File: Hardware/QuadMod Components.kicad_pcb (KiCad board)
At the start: 2 copper layers, 70.6 x 100 mm, 120 parts, among them J1 Conn_01x08_Pin, J2 Conn_01x08_Pin, J3 Conn_01x08_Pin, J4 Conn_01x08_Pin, J5 Eurorack_10_pin_power, J6 USB_B_Micro, J7 Prog_Header, J8 Extra_Outs, U1 LD1117-3.3-4Tab, U2 STM32H563VIT, U3 TL072, U4 MCP6004, U5 TPS561201, U6 MCP6004, U7 MCP6002-xSN, U8 STF202-22T1G, U9 AK4619VN, Y1 8MHz 20pF

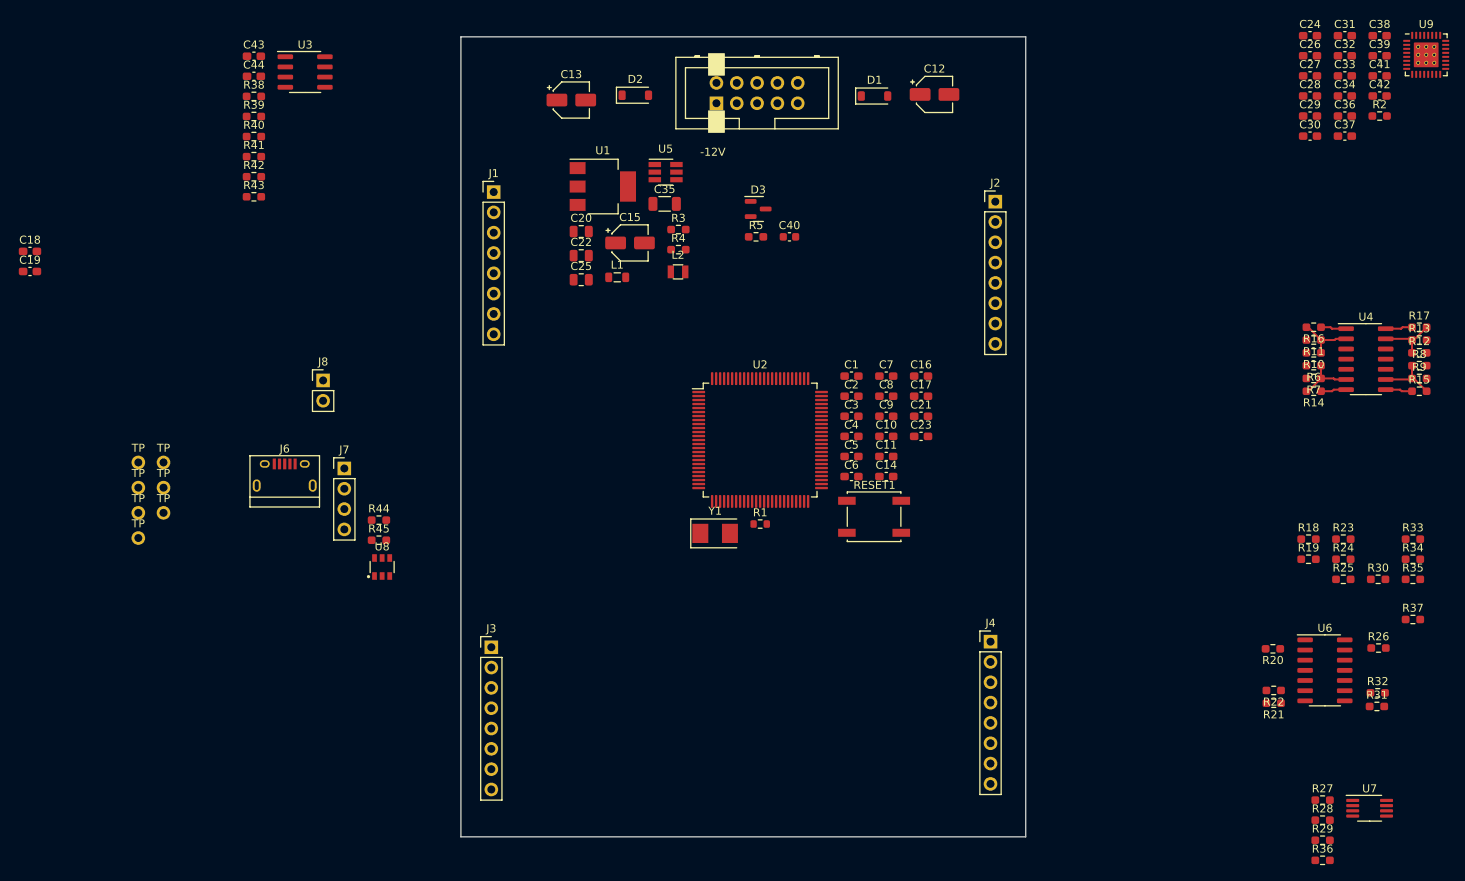
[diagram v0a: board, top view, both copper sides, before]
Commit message: Preliminary component routing
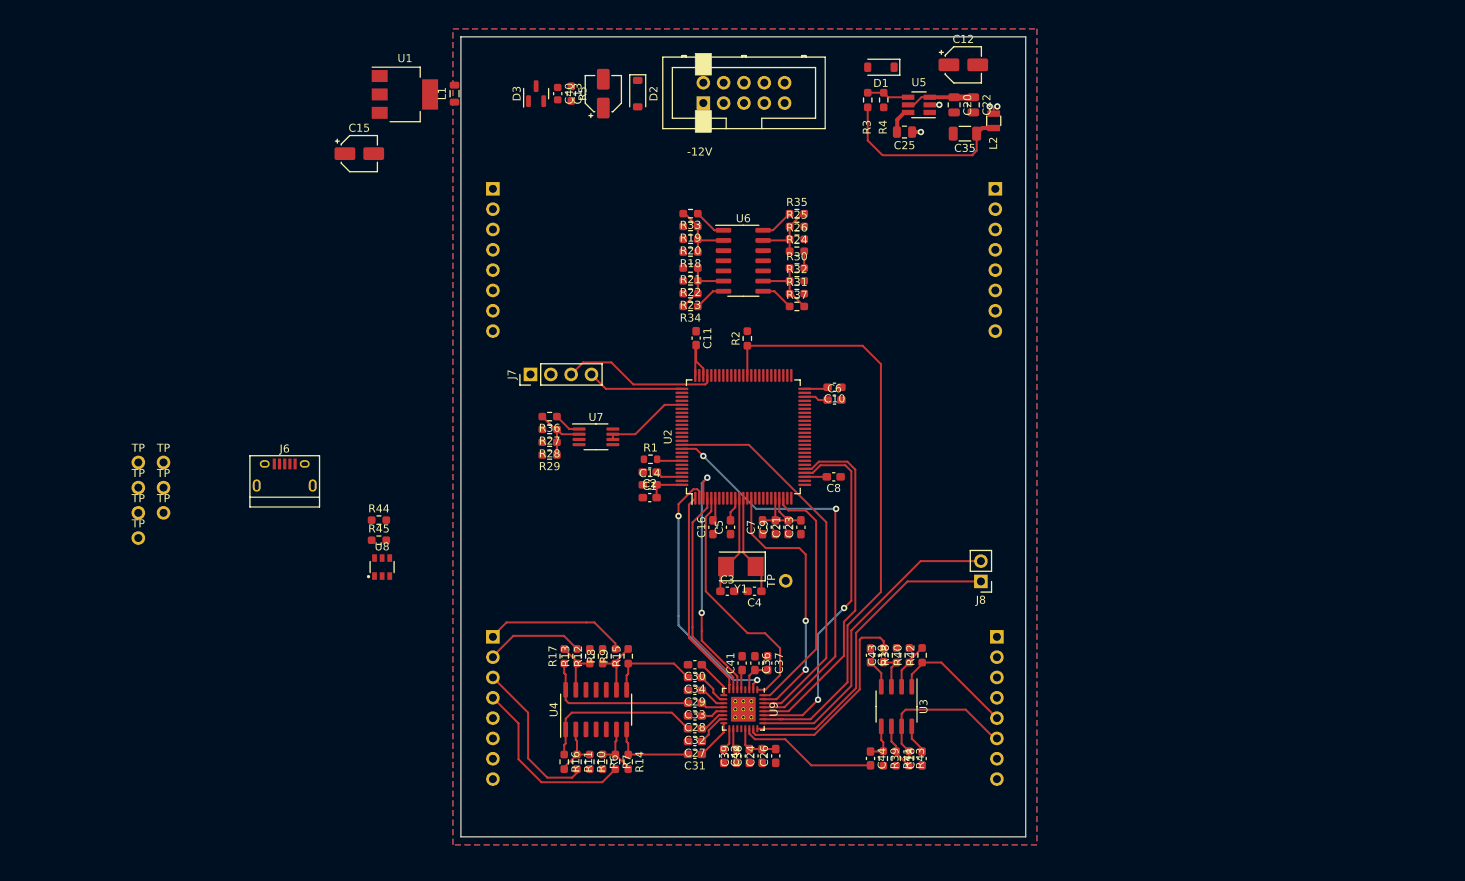
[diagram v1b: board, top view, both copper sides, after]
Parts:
- removed C17: 100nF, Capacitor_SMD:C_0603_1608Metric_Pad1.08x0.95mm_HandSolder
- removed RESET1: SW_Push, Custom_Footprints:SW_SPST_EVQQ2
- added TP8: Reset, Custom_Footprints:1mm_Test_Point, F.Cu at (140.6, 118.0)
- J1, J2, J3, J4: moved to B.Cu
- moved C18 128.3 mm to (157.7, 140.2), turned to 90 degrees
- moved C31 121.1 mm to (129.2, 139.7), turned to 180 degrees
- moved C38 119.6 mm to (136.1, 139.9), turned to 90 degrees
- moved C39 118.8 mm to (134.4, 139.9), turned to 90 degrees
- moved U9 118.2 mm to (135.3, 134.1), turned to -90 degrees
- moved C32 116.9 mm to (129.2, 136.5), turned to 180 degrees
- moved C42 116.3 mm to (132.8, 139.9), turned to -90 degrees
- moved C19 115.5 mm to (151.2, 127.3), turned to -90 degrees
- moved C44 114.9 mm to (151.2, 140.2), turned to -90 degrees
- moved R17 114.5 mm to (112.9, 127.4), turned to 90 degrees
- moved C27 113.3 mm to (129.2, 138.1), turned to 180 degrees
- moved C24 113.1 mm to (137.7, 139.9), turned to 90 degrees
- moved C33 112.9 mm to (129.2, 133.3), turned to 180 degrees
- moved R13 112.5 mm to (114.5, 127.4), turned to 90 degrees
- moved R39 112.4 mm to (152.8, 140.2), turned to -90 degrees
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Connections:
- C43 pad 2: /Audio_Out1 -> /Audio_Out2
- C44 pad 2: /Audio_Out2 -> /Audio_Out1
- J3 pad 1: /FX_TYPE -> /IN4
- J3 pad 2: /CLOCK -> /IN3
- J3 pad 3: /DELAY_LED -> /IN2
- J3 pad 4: /FX_LED -> /IN1
- J4 pad 1: /IN1 -> /FX_TYPE
- J4 pad 2: /IN2 -> /CLOCK
- J4 pad 3: /IN3 -> /DELAY_LED
- J4 pad 4: /IN4 -> /FX_LED
- J4 pad 5: /OUT_AMP1 -> /OUT_AMP2
- J4 pad 6: /OUT_AMP2 -> /OUT_AMP1
- R42 pad 1: /OUT_AMP1 -> /OUT_AMP2
- R43 pad 1: /OUT_AMP2 -> /OUT_AMP1
- U2 pad 15: /LFO_RANGE -> /SAI2_SD_A
- U2 pad 16: /Delay_Time -> unconnected-(U2-PC1-Pad16)
- U2 pad 17: /FX_MIX -> unconnected-(U2-PC2_C-Pad17)
- U2 pad 18: /FX_Feedback -> unconnected-(U2-PC3_C-Pad18)
- U2 pad 23: unconnected-(U2-PA0-Pad23) -> /SAI2_SD_B
- U2 pad 24: unconnected-(U2-PA1-Pad24) -> /FX_Feedback
- U2 pad 25: unconnected-(U2-PA2-Pad25) -> /LFO_RANGE
- U2 pad 26: unconnected-(U2-PA3-Pad26) -> /FX_MIX
- U2 pad 29: unconnected-(U2-PA4-Pad29) -> /SPI1_NSS
- U2 pad 31: unconnected-(U2-PA6-Pad31) -> /Delay_Time
- U2 pad 42: /SAI2_SD_B -> unconnected-(U2-PE11-Pad42)
- U2 pad 58: /SAI2_SD_A -> unconnected-(U2-PD11-Pad58)
- U2 pad 77: /SPI1_NSS -> unconnected-(U2-PA15-Pad77)
- U3 pad 1: /OUT_AMP1 -> /OUT_AMP2
- U3 pad 7: /OUT_AMP2 -> /OUT_AMP1
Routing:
- net /PDN: track 0.00 -> 75.8 mm
- net /SPI1_MOSI: track 0.00 -> 52.6 mm, vias 0 -> 2
- net +3.3V: track 0.00 -> 52.0 mm
- net /SPI1_MISO: track 0.00 -> 49.3 mm
- net /SPI1_NSS: track 0.00 -> 44.5 mm, vias 0 -> 2
- net /SPI1_SCK: track 0.00 -> 44.0 mm
- net /Audio_Out4: track 0.00 -> 39.7 mm
- net /Audio_Out3: track 0.00 -> 39.6 mm
- net /SAI2_SD_A: track 0.00 -> 33.6 mm, vias 0 -> 2
- net /SAI1_SD_B: track 0.00 -> 33.6 mm, vias 0 -> 2
- net /SAI1_FS_A: track 0.00 -> 31.4 mm, vias 0 -> 2
- net /SAI1_SD_A: track 0.00 -> 31.1 mm
- net /SAI2_SD_B: track 0.00 -> 30.9 mm
- net /SAI1_SCK_A: track 0.00 -> 26.8 mm
- net /Audio_Out2: track 0.00 -> 26.7 mm
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- added copper zone on In1.Cu, net /VSW
- added copper zone on B.Cu, net GND
- added copper zone on F.Cu, net GND
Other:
- copper layers 2 -> 4

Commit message: First pass signal routing of component board
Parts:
- moved R45 74.6 mm to (159.3, 85.9)
- moved R44 74.3 mm to (159.3, 84.3)
- moved J6 26.7 mm to (104.2, 109.4), turned to -90 degrees
- moved U8 21.5 mm to (110.5, 109.4), turned to 90 degrees
- moved J8 2.00 mm to (167.0, 118.1)
- moved C11 0.55 mm to (129.3, 88.2)
- moved R2 0.50 mm to (135.8, 88.2)
- moved R1 0.10 mm to (123.6, 102.8)
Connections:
- J1 pad 1: /DLY_TIME_POT -> /DLY_TIME_CV
- J1 pad 2: /DLY_FILTER_CV -> /DLY_TIME_POT
- J1 pad 3: /DLY_FILTER_POT -> /DLY_FILTER_CV
- J1 pad 4: /LFO_SPEED_CV -> /DLY_FILTER_POT
- J1 pad 5: /LFO_SPEED_POT -> /LFO_BASEFREQ_CV
- J1 pad 6: /LFO_RANGE -> /LFO_BASEFREQ_POT
- J1 pad 7: +3.3VA -> /CLOCK
- J2 pad 2: /DLY_FEEDBACK -> /FX_FEEDBACK_CV
- J2 pad 3: /DLY_TIME_CV -> /FX_FEEDBACK_POT
- J2 pad 4: /FX_FEEDBACK_CV -> /LFO_SPEED_POT
- J2 pad 5: /FX_FEEDBACK_POT -> /LFO_SPEED_CV
- J2 pad 6: /LFO_BASEFREQ_CV -> /DELAY_LED
- J2 pad 7: /LFO_BASEFREQ_POT -> /FX_LED
- J3 pad 1: /IN4 -> /FX_TYPE
- J3 pad 2: /IN3 -> /LFO_RANGE
- J3 pad 3: /IN2 -> /IN4
- J3 pad 4: /IN1 -> /IN3
- J3 pad 5: /DLY_MIX -> /IN2
- J3 pad 6: /FX_MIX -> /IN1
- J4 pad 1: /FX_TYPE -> /DLY_FEEDBACK
- J4 pad 2: /CLOCK -> /DLY_MIX
- J4 pad 3: /DELAY_LED -> unconnected-(J4-Pin_3-Pad3)
- J4 pad 4: /FX_LED -> /FX_MIX
- U2 pad 24: /FX_Feedback -> /LFO_Base_Freq
- U2 pad 31: /Delay_Time -> /DLY_FEEDBACK
- U2 pad 32: /Delay_Filter -> /DLY_MIX
- U2 pad 34: /DLY_MIX -> /FX_Feedback
- U2 pad 35: /DLY_FEEDBACK -> /Delay_Time
- U2 pad 36: /LFO_Base_Freq -> /Delay_Filter
- U2 pad 78: /FX_TYPE -> unconnected-(U2-PC10-Pad78)
- U2 pad 87: unconnected-(U2-PD6-Pad87) -> /FX_TYPE
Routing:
- net /LFO_RANGE: track 0.00 -> 48.6 mm, vias 0 -> 2
- net /DLY_MIX: track 0.00 -> 46.3 mm
- net /DLY_FEEDBACK: track 0.00 -> 42.5 mm
- net /FX_Feedback: track 4.17 -> 45.9 mm
- net /FX_MIX: track 0.00 -> 41.2 mm, vias 0 -> 1
- net /Delay_Time: track 4.07 -> 45.2 mm
- net /FX_TYPE: track 0.00 -> 36.9 mm
- net /Delay_Filter: track 4.00 -> 38.0 mm
- net /CLOCK: track 0.00 -> 31.8 mm
- net /LFO_Base_Freq: track 3.41 -> 33.6 mm, vias 0 -> 2
- net /LFO_Speed: track 4.10 -> 33.6 mm
- net /USB_DM: track 0.00 -> 28.2 mm, vias 0 -> 2
- net /USB_DP: track 0.00 -> 27.6 mm, vias 0 -> 2
- net /DLY_FILTER_CV: track 0.00 -> 26.4 mm
- net /DLY_FILTER_POT: track 0.00 -> 26.1 mm
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
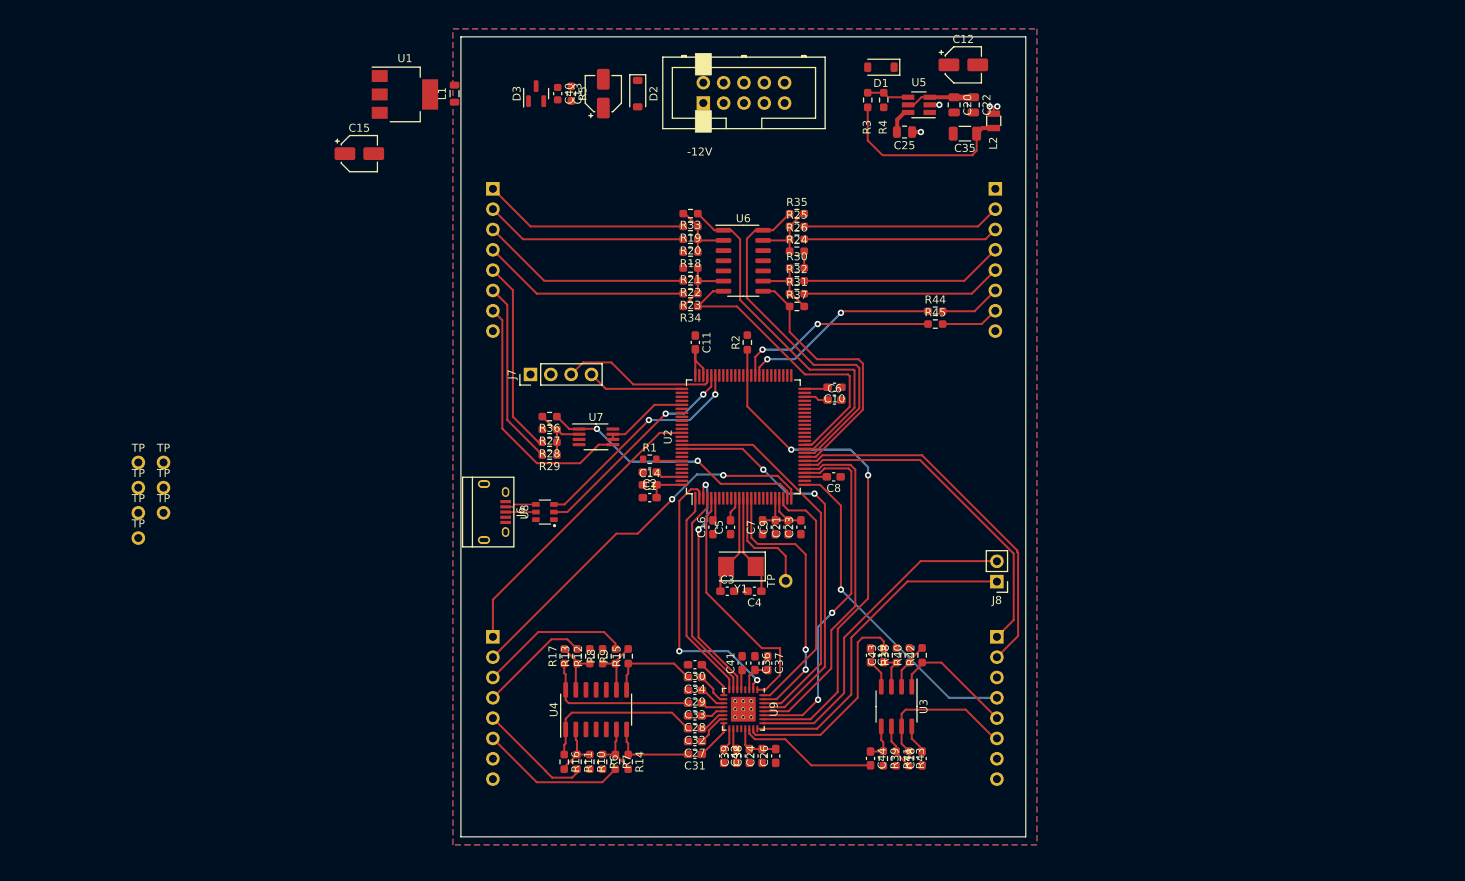
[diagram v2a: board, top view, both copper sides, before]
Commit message: First draft of power routing completed
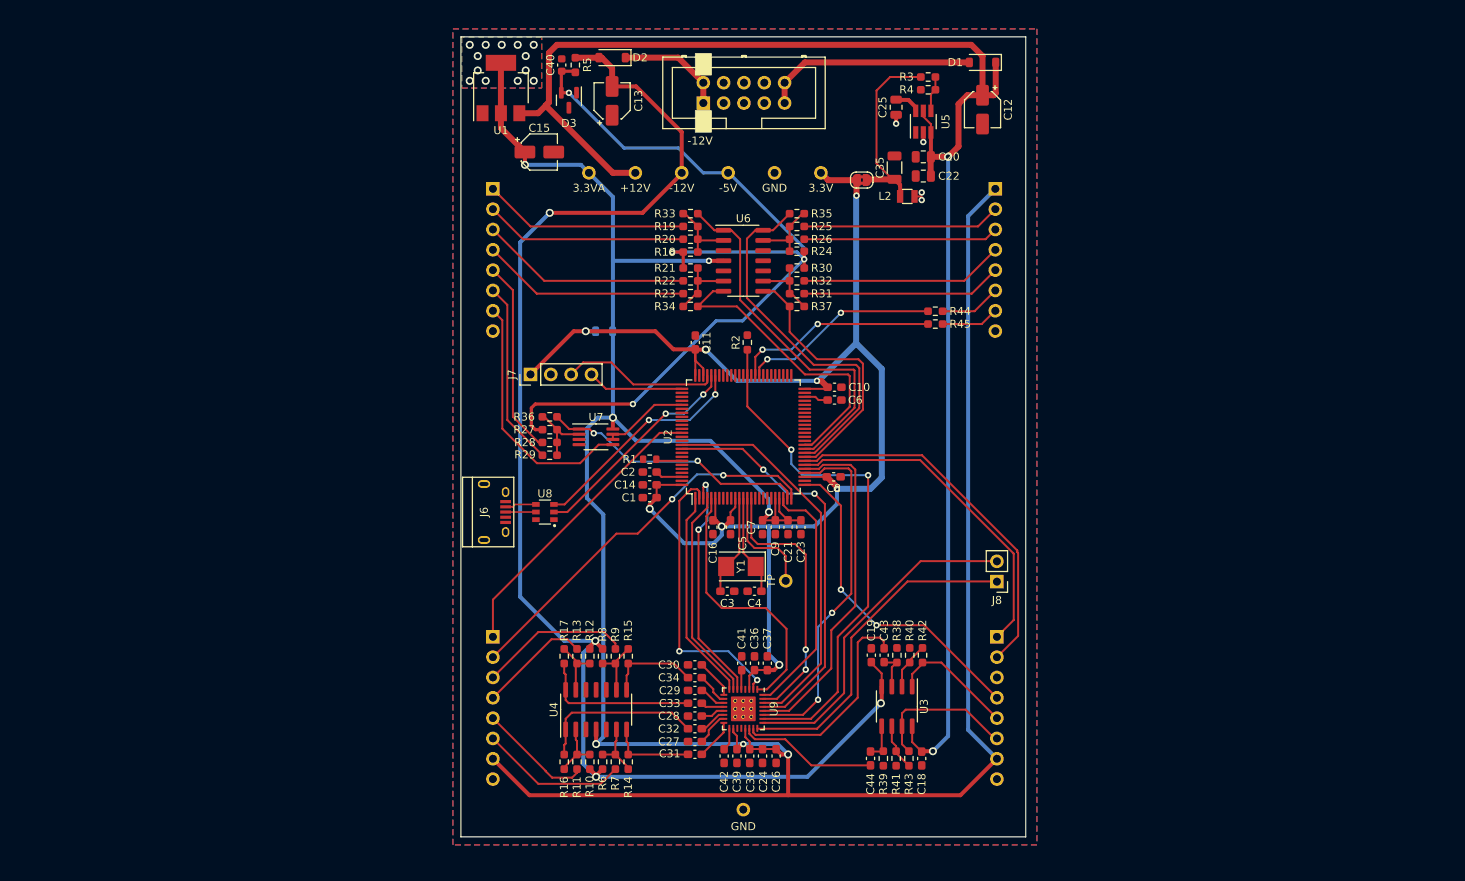
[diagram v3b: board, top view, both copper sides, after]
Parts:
- added JP2: Jumper, Jumper:SolderJumper-2_P1.3mm_Bridged2Bar_RoundedPad1.0x1.5mm, F.Cu at (150.1, 67.9)
- L1: moved to B.Cu
- moved TP5 89.8 mm to (145.0, 67.0)
- moved TP6 85.9 mm to (139.2, 67.0)
- moved TP1 82.1 mm to (133.4, 67.0)
- moved TP7 81.4 mm to (135.3, 146.6)
- moved TP3 80.1 mm to (127.6, 67.0)
- moved TP2 73.5 mm to (121.8, 67.0)
- moved TP4 72.5 mm to (116.0, 67.0)
- moved L1 35.1 mm to (117.9, 86.8), turned to 0 degrees
- moved C15 22.5 mm to (109.8, 64.4)
- moved L2 14.4 mm to (155.8, 70.0), turned to 180 degrees
- moved D1 12.7 mm to (165.2, 53.2)
- moved U1 12.0 mm to (105.0, 56.4), turned to 90 degrees
- moved C22 10.9 mm to (157.8, 67.4), turned to 180 degrees
- moved C35 9.77 mm to (154.2, 66.3), turned to 90 degrees
- moved R3 8.08 mm to (158.4, 55.0), turned to 0 degrees
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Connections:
- C35 pad 1: +3.3V -> Net-(JP2-A)
- L1 pad 1: +3.3VA -> +3.3V
- L1 pad 2: /VO -> +3.3VA
- L2 pad 2: +3.3V -> Net-(JP2-A)
- R3 pad 1: +3.3V -> Net-(JP2-A)
- U1 pad 2: /VO -> +3.3VA
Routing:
- net +3.3VA: track 19.0 -> 334.8 mm, vias 0 -> 20
- net +12V: track 12.3 -> 192.9 mm, vias 0 -> 2
- net -12V: track 3.62 -> 172.2 mm, vias 0 -> 4
- net +3.3V: track 51.0 -> 183.5 mm, vias 0 -> 8
- net /-5V_REF: track 2.10 -> 112.3 mm, vias 0 -> 4
- net /+12V_IN: track 0.00 -> 26.7 mm
- net Net-(JP2-A): track 0.00 -> 24.3 mm
- net /-12V_IN: track 0.00 -> 13.6 mm
- net /SAI1_SD_A: track 31.1 -> 33.7 mm
- net /FB: track 5.28 -> 4.46 mm
- net /FX_MIX: vias 1 -> 2
- added copper zone on B.Cu, net +3.3VA
- added copper zone on F.Cu, net +3.3VA
- added copper zone on In1.Cu, net +3.3VA
- added copper zone on In2.Cu, net +3.3VA

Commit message: Basic layout complete
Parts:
- JP2: footprint Jumper:SolderJumper-2_P1.3mm_Bridged2Bar_RoundedPad1.0x1.5mm -> Jumper:SolderJumper-2_P1.3mm_Open_RoundedPad1.0x1.5mm
- moved TP7 58.7 mm to (167.0, 97.2)
- moved R44 3.40 mm to (155.9, 84.3)
- moved R45 3.40 mm to (155.9, 85.9)
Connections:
- net Net-(JP2-A) renamed /D3V3
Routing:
- net GND: track 0.00 -> 25.5 mm, vias 0 -> 73
- net +3.3V: track 183.5 -> 201.2 mm
- net +3.3VA: track 334.8 -> 339.2 mm
- net /FX_LED: track 7.28 -> 10.7 mm
- net /DELAY_LED: track 7.66 -> 11.1 mm
- net /Delay_Led_Out: track 25.0 -> 21.6 mm
- net /FX_Led_Out: track 25.6 -> 22.2 mm
- net /-5V_REF: track 112.3 -> 109.7 mm
- net /SAI2_SD_A: track 33.9 -> 32.1 mm
- net -12V: track 172.2 -> 173.9 mm
- net /SPI1_SCK: track 43.6 -> 45.2 mm
- net /LFO_RANGE: track 48.6 -> 50.1 mm
- net /PDN: track 66.2 -> 65.2 mm
- net /LFO_Speed: track 33.6 -> 34.4 mm
- net /Audio_Out2: track 27.0 -> 27.9 mm
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- added copper zone on In1.Cu, net GND
- added copper zone on In2.Cu, net GND
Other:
- board text added: "3V3"
- board text added: "CLK"
- board text added: "DAC3"
- board text added: "DAC4"
- board text added: "GND"
- board text added: "IO"
- board text added: "J1"
- board text added: "J2"
- board text added: "J3"
- board text added: "J4"

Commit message: First draft of control board
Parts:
- removed R29: 47k, Resistor_SMD:R_0603_1608Metric_Pad0.98x0.95mm_HandSolder
- moved J3 1.91 mm to (102.7, 123.6)
- moved J4 1.66 mm to (167.9, 123.6)
- moved J1 1.30 mm to (102.7, 69.0)
- moved J2 1.10 mm to (167.9, 69.0)
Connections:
- J1 pad 1: /DLY_TIME_CV -> /LFO_BASEFREQ_CV
- J1 pad 2: /DLY_TIME_POT -> /LFO_BASEFREQ_POT
- J1 pad 5: /LFO_BASEFREQ_CV -> GND
- J1 pad 6: /LFO_BASEFREQ_POT -> /DLY_TIME_POT
- J1 pad 7: /CLOCK -> /DLY_TIME_CV
- J3 pad 2: /LFO_RANGE -> /DLY_FEEDBACK
- J4 pad 1: /DLY_FEEDBACK -> /LFO_RANGE
- J4 pad 3: unconnected-(J4-Pin_3-Pad3) -> +3.3VA
- J4 pad 7: +3.3VA -> GND
- R19 pad 2: /DLY_TIME_CV -> /LFO_BASEFREQ_CV
- R20 pad 2: /DLY_TIME_POT -> /LFO_BASEFREQ_POT
- R28 pad 2: /LFO_BASEFREQ_CV -> /DLY_TIME_CV
- R33 pad 1: /Delay_Time -> /LFO_Base_Freq
- R36 pad 1: /LFO_Base_Freq -> /Delay_Time
- U2 pad 16: unconnected-(U2-PC1-Pad16) -> /DLY_TIME_POT
- U2 pad 24: /LFO_Base_Freq -> /Delay_Time
- U2 pad 25: /LFO_RANGE -> /DLY_FEEDBACK
- U2 pad 31: /DLY_FEEDBACK -> /LFO_RANGE
- U2 pad 35: /Delay_Time -> /LFO_Base_Freq
- U6 pad 1: /Delay_Time -> /LFO_Base_Freq
- U7 pad 1: /LFO_Base_Freq -> /Delay_Time
- U7 pad 5: /CLOCK -> /DLY_TIME_CV
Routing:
- net /CLOCK: track 31.8 -> 0.00 mm
- net /DLY_TIME_POT: track 25.3 -> 53.7 mm, vias 0 -> 2
- net /LFO_Base_Freq: track 33.6 -> 46.0 mm, vias 2 -> 0
- net /Delay_Time: track 46.0 -> 33.6 mm, vias 0 -> 2
- net /DLY_FEEDBACK: track 42.5 -> 50.9 mm, vias 0 -> 2
- net +3.3VA: track 339.2 -> 345.6 mm, vias 20 -> 21
- net /LFO_RANGE: track 50.1 -> 44.1 mm, vias 2 -> 0
- net /DLY_TIME_CV: track 25.7 -> 29.7 mm
- net /LFO_BASEFREQ_POT: track 23.2 -> 26.6 mm
- net /LFO_BASEFREQ_CV: track 24.4 -> 27.1 mm
- net /IN2: track 14.3 -> 16.2 mm
- net /IN1: track 18.4 -> 20.3 mm
- net /DLY_MIX: track 46.3 -> 48.0 mm
- net Net-(U7A--): track 8.69 -> 7.08 mm
- net /DLY_FILTER_CV: track 26.4 -> 27.8 mm
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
